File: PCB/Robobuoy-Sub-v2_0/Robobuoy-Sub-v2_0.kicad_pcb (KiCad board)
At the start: 4 copper layers, 80 x 104.1 mm, 141 parts, among them J101 PROG/JTAG, J102 PUSH BUTTON, J103 RS232_Option, J104 ESC_BB, J105 ESC_SB, J106 Compass, J201 Accu 1, J202 LoadbalanceAccu1, J203 LoadbalanceAccu2, J204 CHARGE/ON-OFF, J205 Accu 2, J206 ESCSB, J207 ESCBB, Q101 AO3400A, Q102 AO3400A, Q201 AO3400A, Q202 AO3400A, Q203 AO3400A, Q204 AO3400A, Q205 AO3400A, Q206 AO3400A, Q207 AO3400A, Q208 AO3400A, SW101 ~{BOOT}, SW102 ~{RESET}, SW103 MODE, SW201 On/Off, U101 ESP32-WROOM-32E_(visible_peri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, U102 USBLC6-4SC6, U103 LSM303AGRTR, U104 LTC4311, U105 SN74LV1T34DBV, U106 SN74LV1T34DBV, U201 TPS5430DDAR, U202 SN74LV1T34DBV, U203 SN74LV1T34DBV, U204 TLV61046ADB

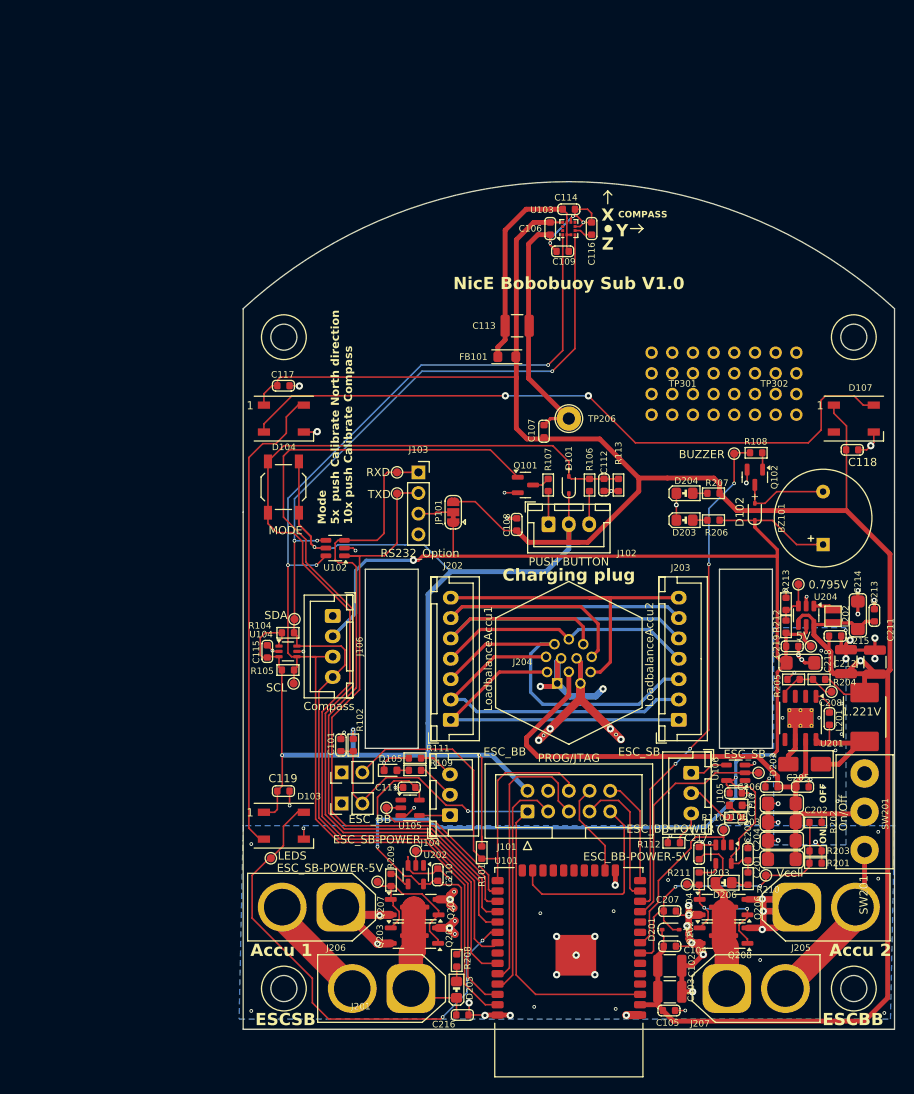
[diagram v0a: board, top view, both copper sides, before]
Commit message: Struct re defined. not finished yet
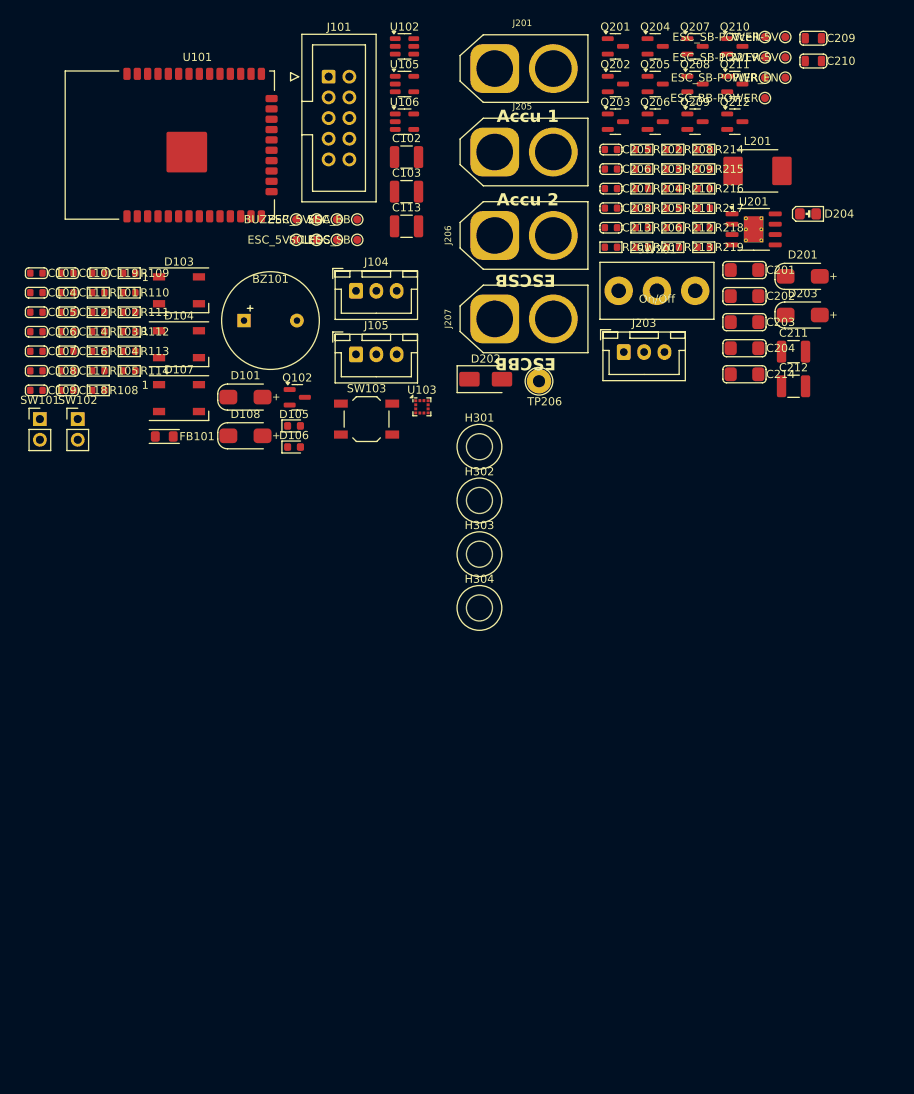
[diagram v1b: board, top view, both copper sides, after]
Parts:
- removed C115, C215, C216, C217, C219: 100n, A_Device:C_0603
- removed C218: 4.7uF/10V, A_Device:C_1206_(1.6)
- removed D102: 1N4148WS, A_Device:D_SOD-323_1.8x1.4x1.15
- removed D205: ESC_BB, A_Passive:LED_0805
- removed D206: ESC_SB, A_Passive:LED_0805
- removed J102: PUSH BUTTON, Connector_JST:JST_XH_B3B-XH-A_1x03_P2.50mm_Vertical
- removed J103: RS232_Option, Connector_PinSocket_2.54mm:PinSocket_1x04_P2.54mm_Vertical
- removed J106: Compass, Connector_JST:JST_XH_B4B-XH-A_1x04_P2.50mm_Vertical
- removed J202: LoadbalanceAccu1, Connector_JST:JST_XH_B7B-XH-A_1x07_P2.50mm_Vertical
- removed J204: CHARGE/ON-OFF, A_Connector:T4140012121000
- removed JP101: 5V/3.3V, Jumper:SolderJumper-3_P1.3mm_Bridged12_RoundedPad1.0x1.5mm
- removed L202: 10uH, A_Device:FTC252012S
- removed Q101: AO3400A, Package_TO_SOT_SMD:SOT-23
- removed R106, R107: 100, A_Device:R_0603
- removed TP209: 0.795V, A_Pads_Pins:Testpad_1
- removed TP210: 5V, A_Pads_Pins:Testpad_1
- removed TP301: RW1, A_Misc:ReworkPins
- removed TP302: RW2, A_Misc:ReworkPins
- removed U104: LTC4311, Package_TO_SOT_SMD:Texas_R-PDSO-G6
- removed U202, U203: SN74LV1T34DBV, Package_TO_SOT_SMD:SOT-23-5
- removed U204: TLV61046ADB, Package_TO_SOT_SMD:SOT-23-6
- added D108: SS14, A_Device:D_SMA_4.3x3x2.4, F.Cu at (86.1, 70.0)
- added Q209: AO3401A, Package_TO_SOT_SMD:SOT-23, F.Cu at (141.3, 31.4)
- added Q210: AO3401A, Package_TO_SOT_SMD:SOT-23, F.Cu at (146.2, 22.2)
- added Q211: AO3401A, Package_TO_SOT_SMD:SOT-23, F.Cu at (146.2, 26.8)
- added Q212: AO3400A, Package_TO_SOT_SMD:SOT-23, F.Cu at (146.2, 31.4)
- added R103: 100, A_Device:R_0603, F.Cu at (68.0, 57.2)
- added R114: 100, A_Device:R_0603, F.Cu at (71.8, 62.0)
- added R214: 10K, A_Device:R_0603, F.Cu at (142.4, 34.8)
- added R215: 10K, A_Device:R_0603, F.Cu at (142.4, 37.2)
- added R216: 100K, A_Device:R_0603, F.Cu at (142.4, 39.6)
- added R217: 100, A_Device:R_0603, F.Cu at (142.4, 42.0)
- added R218: 100K, A_Device:R_0603, F.Cu at (142.4, 44.4)
- added R219: 100K, A_Device:R_0603, F.Cu at (142.4, 46.8)
- added TP205: ESC_SB-POWER-5V, A_Pads_Pins:Testpad_1, F.Cu at (152.4, 21.0)
- C209, C210: value 100n -> 10u/25V; footprint A_Device:C_0603 -> A_Device:C_0805
- D101, D201: value 1N4148WS -> SS14; footprint A_Device:D_SOD-323_1.8x1.4x1.15 -> A_Device:D_SMA_4.3x3x2.4
- D106: value PWR_ESC_BB -> PWR_ESC_SB
- D203: value 5V -> SS14; footprint A_Passive:LED_0805 -> A_Device:D_SMA_4.3x3x2.4
- J203: value LoadbalanceAccu2 -> CHRG_DATA; footprint Connector_JST:JST_XH_B7B-XH-A_1x07_P2.50mm_Vertical -> Connector_JST:JST_XH_B3B-XH-A_1x03_P2.50mm_Vertical
- Q203, Q204, Q205, Q206, Q207, Q208: value AO3400A -> AO3401A
- R109, R110: value 1.8k -> 4.7k
- R206, R210: value 1.8k -> 10K
- R207: value 1k -> 100
- R208: value 1.8k -> 100K
- R211: value 100 -> 10K
- R212: value 82K -> 100K
- R213: value 15K -> 100K
- TP102: value RXD -> ESC_5V
- TP103: value TXD -> ESC_5V
- TP208: value ESC_BB-POWER-5V -> PWR_EN
- moved C105 115.7 mm to (60.4, 54.8)
- moved TP207 113.0 mm to (152.4, 23.5)
- moved U101 112.8 mm to (76.8, 34.3), turned to 0 degrees
- moved Q207 111.8 mm to (141.3, 22.2)
- moved C104 111.8 mm to (60.4, 52.4)
- moved Q201 111.6 mm to (131.5, 22.2), turned to 0 degrees
- moved C210 110.1 mm to (155.8, 24.0), turned to 0 degrees
- moved Q204 105.9 mm to (136.4, 22.2)
- moved Q202 105.2 mm to (131.5, 26.8)
- moved Q205 104.8 mm to (136.4, 26.8), turned to 0 degrees
- moved Q208 104.7 mm to (141.3, 26.8), turned to 0 degrees
- moved J201 104.7 mm to (116.7, 24.9), turned to 0 degrees
- moved C102 104.5 mm to (105.9, 35.8)
- moved TP203 104.2 mm to (149.9, 26.0)
- moved C110 104.0 mm to (64.2, 50.0)
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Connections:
- net /CPU/SCL renamed Net-(U101-SCL/GPIO22)
- net /CPU/SDA renamed Net-(U101-SDA/GPIO21)
- BZ101 pad 1: +5V -> +3.3V
- C110 pad 1: +5V -> Net-(J105-Pin_2)
- C110 pad 2: GND -> Net-(D106-K)
- C111 pad 1: +5V -> Net-(J104-Pin_2)
- C111 pad 2: GND -> Net-(D105-K)
- C201 pad 1: +VSW -> Vbatt
- C202 pad 1: +VSW -> Vbatt
- C203 pad 1: +VSW -> Vbatt
- C204 pad 1: +VSW -> Vbatt
- C205 pad 1: +VSW -> Vbatt
- C206 pad 1: +VSW -> Vbatt
- C209 pad 1: +5V -> Net-(D203-K)
- C210 pad 1: +5V -> Net-(D203-K)
- D101 pad 2: BUTTON -> Net-(BZ101--)
- D105 pad 1: GND -> Net-(D105-K)
- D106 pad 1: GND -> Net-(D106-K)
- D203 pad 1: GND -> Net-(D203-K)
- D203 pad 2: Net-(D203-A) -> /CPU/COM
- J104 pad 3: Net-(J104-Pin_3) -> Net-(D105-K)
- J105 pad 3: Net-(J105-Pin_3) -> Net-(D106-K)
- J203 pad 1: Net-(J202-Pin_1) -> GND
- J203 pad 2: Net-(J202-Pin_2) -> /CPU/COM
- J203 pad 3: Net-(J202-Pin_3) -> Vbatt
- J206 pad 1: Net-(D205-K) -> GND
- J206 pad 2: Vbatt -> Net-(J206-Pin_2)
- J207 pad 1: Net-(D206-K) -> GND
- J207 pad 2: Vbatt -> Net-(J207-Pin_2)
- Q201 pad 3: Net-(D205-K) -> Net-(Q201-D)
- Q202 pad 3: Net-(D206-K) -> Net-(Q202-D)
- Q203 pad 1: Net-(Q201-G) -> Net-(Q203-G)
- Q203 pad 2: GND -> Vbatt
- Q203 pad 3: Net-(D205-K) -> Net-(J206-Pin_2)
- Q204 pad 1: Net-(Q202-G) -> Net-(Q204-G)
- Q204 pad 2: GND -> Vbatt
- Q204 pad 3: Net-(D206-K) -> Net-(J207-Pin_2)
- Q205 pad 1: Net-(Q201-G) -> Net-(Q203-G)
- Q205 pad 2: GND -> Vbatt
- Q205 pad 3: Net-(D205-K) -> Net-(J206-Pin_2)
- Q206 pad 1: Net-(Q202-G) -> Net-(Q204-G)
- Q206 pad 2: GND -> Vbatt
- Q206 pad 3: Net-(D206-K) -> Net-(J207-Pin_2)
- Q207 pad 1: Net-(Q201-G) -> Net-(Q203-G)
- Q207 pad 2: GND -> Vbatt
- Q207 pad 3: Net-(D205-K) -> Net-(J206-Pin_2)
- Q208 pad 1: Net-(Q202-G) -> Net-(Q204-G)
- Q208 pad 2: GND -> Vbatt
- Q208 pad 3: Net-(D206-K) -> Net-(J207-Pin_2)
- R111 pad 2: Net-(J104-Pin_3) -> Net-(D105-K)
- R112 pad 2: Net-(J105-Pin_3) -> Net-(D106-K)
- R202 pad 1: +VSW -> Net-(Q211-D)
- R206 pad 1: +5V -> Net-(D204-A)
- R206 pad 2: Net-(D203-A) -> +3.3V
- R207 pad 1: Net-(D204-A) -> Net-(Q202-G)
- R207 pad 2: +3.3V -> /CPU/PWR_ESC_BB
- R208 pad 1: +5V -> Net-(D203-K)
- R208 pad 2: Net-(D205-A) -> GND
- R209 pad 2: Net-(U202-Y) -> /CPU/PWR_ESC_SB
- R210 pad 1: +5V -> Net-(Q202-D)
- R210 pad 2: Net-(D206-A) -> Net-(Q204-G)
- R211 pad 1: Net-(Q202-G) -> Vbatt
- R211 pad 2: Net-(U203-Y) -> Net-(Q204-G)
- R212 pad 1: +5V -> Net-(D203-K)
- R212 pad 2: Net-(U204-FB) -> Net-(R212-Pad2)
- R213 pad 1: Net-(U204-FB) -> Net-(R213-Pad1)
- R213 pad 2: GND -> Net-(R212-Pad2)
- SW201 pad 2: +VSW -> Net-(R216-Pad1)
- TP102 pad 1: Net-(J103-Pin_1) -> Net-(J104-Pin_2)
- TP103 pad 1: Net-(J103-Pin_2) -> Net-(J105-Pin_2)
- TP107 pad 1: ESC_BB -> Net-(U105-A)
- TP108 pad 1: ESC_SB -> Net-(U106-A)
- TP207 pad 1: Net-(Q201-G) -> Net-(Q203-G)
- TP208 pad 1: Net-(Q202-G) -> Net-(D203-K)
- U101 pad 27: Net-(J103-Pin_2) -> /CPU/VbatEn
- U101 pad 28: Net-(J103-Pin_1) -> /CPU/COM
- U101 pad 29: BUTTON_LIGHT -> unconnected-(U101-CS/GPIO5-Pad29)
- U102 pad 1: Net-(J103-Pin_2) -> /CPU/COM
- U102 pad 3: Net-(J103-Pin_1) -> /CPU/COM
- U105 pad 2: ESC_BB -> Net-(U105-A)
- U105 pad 3: GND -> Net-(D105-K)
- U105 pad 5: +5V -> Net-(J104-Pin_2)
- U106 pad 2: ESC_SB -> Net-(U106-A)
- U106 pad 3: GND -> Net-(D106-K)
- U106 pad 5: +5V -> Net-(J105-Pin_2)
- U201 pad 5: unconnected-(U201-ENA-Pad5) -> Net-(D203-K)
- U201 pad 7: +VSW -> Vbatt
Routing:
- net +3.3V: track 457.9 -> 0.00 mm, vias 5 -> 0
- net GND: track 247.7 -> 12.2 mm, vias 97 -> 0
- net +5V: track 231.5 -> 0.00 mm, vias 5 -> 0
- net Net-(U101-SCL/GPIO22): track 147.1 -> 0.00 mm, vias 3 -> 0
- net Net-(U101-SDA/GPIO21): track 140.7 -> 0.00 mm, vias 3 -> 0
- net BUTTON: track 129.5 -> 0.00 mm
- net BUTTON_LIGHT: track 108.5 -> 0.00 mm
- net Net-(D104-DOUT): track 84.7 -> 0.00 mm, vias 2 -> 0
- net Net-(J103-Pin_1): track 82.4 -> 0.00 mm
- net Net-(J103-Pin_2): track 77.1 -> 0.00 mm
- net +VSW: track 72.0 -> 0.00 mm
- net EN: track 68.8 -> 0.00 mm, vias 1 -> 0
- net BUZZER: track 62.4 -> 0.00 mm, vias 4 -> 0
- net LEDS: track 60.2 -> 0.00 mm, vias 2 -> 0
- net Vbatt: track 189.9 -> 130.0 mm, vias 6 -> 0
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- removed copper zone on B.Cu, net GND
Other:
- board outline removed
- board text removed: "COMPASS"
- board text removed: "Charging plug"
- board text removed: "Mode 5x push Calibrate North direction 10x push Calibrate Compass"
- board text removed: "NicE Bobobuoy Sub V1.0"
- board text removed: "OFF"
- board text removed: "ON"
- board text removed: "X"
- board text removed: "Y"
- board text removed: "Z"

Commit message: Many changes
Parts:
- removed C118, C119: 100n, A_Device:C_0603
- removed D104, D107: WS2812B, LED_SMD:LED_WS2812B_PLCC4_5.0x5.0mm_P3.2mm
- removed D106: PWR_ESC_SB, LED_SMD:LED_0603_1608Metric
- removed D108: SS14, A_Device:D_SMA_4.3x3x2.4
- removed H301, H302, H303, H304: MountingHole, A_Mechanical:NPTH_M3
- removed J104: ESC_BB, Connector_JST:JST_XH_B3B-XH-A_1x03_P2.50mm_Vertical
- removed J105: ESC_SB, Connector_JST:JST_XH_B3B-XH-A_1x03_P2.50mm_Vertical
- removed J201: Accu 1, A_Connector:AMASS_XT60-M_1x02_P7.20mm_Vertical
- removed J203: CHRG_DATA, Connector_JST:JST_XH_B3B-XH-A_1x03_P2.50mm_Vertical
- removed J205: Accu 2, A_Connector:AMASS_XT60-M_1x02_P7.20mm_Vertical
- removed J206: ESCSB, A_Connector:AMASS_XT60-F_1x02_P7.20mm_Vertical
- removed J207: ESCBB, A_Connector:AMASS_XT60-F_1x02_P7.20mm_Vertical
- removed Q102, Q212: AO3400A, Package_TO_SOT_SMD:SOT-23
- removed Q203, Q204, Q205, Q206, Q207, Q208, Q209, Q210, Q211: AO3401A, Package_TO_SOT_SMD:SOT-23
- removed R108, R111, R112, R114, R217: 100, A_Device:R_0603
- removed R109, R110: 4.7k, A_Device:R_0603
- removed R113, R214, R215: 10K, A_Device:R_0603
- removed R216, R218, R219: 100K, A_Device:R_0603
- removed TP105: SDA, A_Pads_Pins:Testpad_1
- removed TP106: LEDS, A_Pads_Pins:Testpad_1
- removed TP107: ESC_BB, A_Pads_Pins:Testpad_1
- removed TP108: ESC_SB, A_Pads_Pins:Testpad_1
- removed TP205, TP207: ESC_SB-POWER-5V, A_Pads_Pins:Testpad_1
- removed TP206: GND, TestPoint:TestPoint_Loop_D2.54mm_Drill1.5mm_Beaded
- removed TP208: PWR_EN, A_Pads_Pins:Testpad_1
- removed U105, U106: SN74LV1T34DBV, Package_TO_SOT_SMD:SOT-23-5
- added C401: 100n, A_Device:C_0603, F.Cu at (256.3, 49.9)
- added C402: 100n, A_Device:C_0603, F.Cu at (246.4, 62.2)
- added C403: 100n, A_Device:C_0603, F.Cu at (277.2, 92.5)
- added C404: 100n, A_Device:C_0603, F.Cu at (245.8, 112.5)
- added D102: WS2812B, LED_SMD:LED_WS2812B_PLCC4_5.0x5.0mm_P3.2mm, F.Cu at (129.5, 143.8)
- added D205: 3.3V, A_Passive:LED_0805, F.Cu at (61.9, 106.2)
- added D401: SS14, A_Device:D_SMA_4.3x3x2.4, F.Cu at (259.2, 45.9)
- added D402: PWR_ESC_BB, LED_SMD:LED_0603_1608Metric, F.Cu at (246.4, 64.0)
- added D403: SS14, A_Device:D_SMA_4.3x3x2.4, F.Cu at (259.4, 94.9)
- added D404: PWR_ESC_BB, LED_SMD:LED_0603_1608Metric, F.Cu at (252.9, 111.7)
- added H501: MountingHole, A_Mechanical:NPTH_M3, F.Cu at (70.5, 108.1)
- added H502: MountingHole, A_Mechanical:NPTH_M3, F.Cu at (70.5, 114.7)
- added H503: MountingHole, A_Mechanical:NPTH_M3, F.Cu at (70.5, 121.3)
- added H504: MountingHole, A_Mechanical:NPTH_M3, F.Cu at (70.5, 127.9)
- added J102: Conn_01x03_Pin, Connector_Wire:SolderWire-0.75sqmm_1x03_P4.8mm_D1.25mm_OD2.3mm, F.Cu at (141.2, 132.2)
- added J103: Conn_01x03_Pin, Connector_Wire:SolderWire-0.75sqmm_1x03_P4.8mm_D1.25mm_OD2.3mm, F.Cu at (136.0, 140.7)
- added J202: CHRG/DATA, Connector_Wire:SolderWire-0.75sqmm_1x03_P4.8mm_D1.25mm_OD2.3mm, F.Cu at (53.2, 129.6)
- added J401: PWR_ESC_SB, Connector_Wire:SolderWire-0.75sqmm_1x02_P4.8mm_D1.25mm_OD2.3mm, F.Cu at (245.4, 45.9)
- added J402: ESC_SB, Connector_JST:JST_XH_B3B-XH-A_1x03_P2.50mm_Vertical, F.Cu at (250.3, 58.4)
- added J403: INPUT_BB, Connector_Wire:SolderWire-0.75sqmm_1x03_P4.8mm_D1.25mm_OD2.3mm, F.Cu at (264.8, 99.7)
- added J404: INPUT_SB, Connector_Wire:SolderWire-0.75sqmm_1x03_P4.8mm_D1.25mm_OD2.3mm, F.Cu at (264.8, 50.7)
- added J405: ESC_BB, Connector_JST:JST_XH_B3B-XH-A_1x03_P2.50mm_Vertical, F.Cu at (250.3, 106.4)
- added J406: ESCBB, Connector_Wire:SolderWire-0.75sqmm_1x02_P4.8mm_D1.25mm_OD2.3mm, F.Cu at (245.4, 94.9)
- added MOD401: Balanced 6S BMS, A_Module:BMS_6S_14A, F.Cu at (209.8, 46.9)
- added MOD402: ~, A_Mechanical:Accupack_6C, F.Cu at (210.8, 45.9)
- added MOD403: ~, A_Mechanical:Accupack_6C, F.Cu at (210.8, 94.9)
- added MOD404: Balanced 6S BMS, A_Module:BMS_6S_14A, F.Cu at (209.8, 94.9)
- added Q101: AO3400A, Package_TO_SOT_SMD:SOT-23, F.Cu at (146.9, 124.5)
- added Q401: AO3400A, Package_TO_SOT_SMD:SOT-23, F.Cu at (258.8, 49.9)
- added Q402: AO3401A, Package_TO_SOT_SMD:SOT-23, F.Cu at (254.4, 40.8)
- added Q403: AO3401A, Package_TO_SOT_SMD:SOT-23, F.Cu at (243.7, 40.8)
- added Q404: AO3401A, Package_TO_SOT_SMD:SOT-23, F.Cu at (247.3, 40.8)
- added Q405: AO3401A, Package_TO_SOT_SMD:SOT-23, F.Cu at (250.8, 40.8)
- added Q406: AO3401A, Package_TO_SOT_SMD:SOT-23, F.Cu at (258.0, 40.8)
- added Q407: AO3400A, Package_TO_SOT_SMD:SOT-23, F.Cu at (272.8, 89.1)
- added Q408: AO3401A, Package_TO_SOT_SMD:SOT-23, F.Cu at (243.7, 88.9)
- added Q409: AO3401A, Package_TO_SOT_SMD:SOT-23, F.Cu at (247.3, 88.9)
- added Q410: AO3401A, Package_TO_SOT_SMD:SOT-23, F.Cu at (250.8, 88.9)
- added Q411: AO3401A, Package_TO_SOT_SMD:SOT-23, F.Cu at (254.4, 88.9)
- added Q412: AO3401A, Package_TO_SOT_SMD:SOT-23, F.Cu at (257.9, 88.9)
- added R106: 100, A_Device:R_0603, F.Cu at (109.5, 144.6)
- added R401: 100, A_Device:R_0603, F.Cu at (254.8, 47.0)
- added R402: 100K, A_Device:R_0603, F.Cu at (254.8, 49.9)
- added R403: 10K, A_Device:R_0603, F.Cu at (260.8, 40.9)
- added R404: 18K, A_Device:R_0603, F.Cu at (240.2, 45.9)
- added R405: 100, A_Device:R_0603, F.Cu at (265.5, 55.1)
- added R406: 4.7k, A_Device:R_0603, F.Cu at (249.4, 64.0)
- added R407: 100, A_Device:R_0603, F.Cu at (238.8, 57.1)
- added R408: 100K, A_Device:R_0603, F.Cu at (263.9, 55.1)
- added R409: 100, A_Device:R_0603, F.Cu at (272.7, 83.6)
- added R410: 100K, A_Device:R_0603, F.Cu at (277.2, 99.8)
- added R411: 100, A_Device:R_0603, F.Cu at (277.2, 102.2)
- added R412: 10K, A_Device:R_0603, F.Cu at (260.9, 90.1)
- added R413: 100K, A_Device:R_0603, F.Cu at (281.0, 95.0)
- added R414: 18K, A_Device:R_0603, F.Cu at (239.5, 93.7)
- added R415: 4.7k, A_Device:R_0603, F.Cu at (245.9, 110.4)
- added R416: 100, A_Device:R_0603, F.Cu at (238.9, 105.7)
- added TP401: ESC_BB-POWER, A_Pads_Pins:Testpad_1, F.Cu at (253.2, 46.3)
- added TP402: ESC_SB-POWER-5V, A_Pads_Pins:Testpad_1, F.Cu at (240.1, 47.8)
- added TP403: ESC_BB, A_Pads_Pins:Testpad_1, F.Cu at (262.1, 55.8)
- added TP404: ESC_5V, A_Pads_Pins:Testpad_1, F.Cu at (250.2, 65.9)
- added TP405: ESC_BB-POWER, A_Pads_Pins:Testpad_1, F.Cu at (284.1, 100.4)
- added TP406: ESC_BB, A_Pads_Pins:Testpad_1, F.Cu at (284.1, 102.9)
- added TP407: ESC_SB-POWER-5V, A_Pads_Pins:Testpad_1, F.Cu at (284.1, 105.4)
- added TP408: ESC_5V, A_Pads_Pins:Testpad_1, F.Cu at (284.1, 107.9)
- added U401: SN74LV1T34DBV, Package_TO_SOT_SMD:SOT-23-5, F.Cu at (264.5, 59.1)
- added U402: SN74LV1T34DBV, Package_TO_SOT_SMD:SOT-23-5, F.Cu at (288.0, 110.9)
- C102, C103, C113: value 100u/10V -> 100n; footprint Capacitor_SMD:C_1210_3225Metric -> A_Device:C_0603
- C105, C106, C114: value 100n -> 100u/10V; footprint A_Device:C_0603 -> Capacitor_SMD:C_1210_3225Metric
- C117: value 100n -> 10n
- C208: value 10n -> 10u/25V; footprint A_Device:C_0603 -> A_Device:C_0805
- C210: value 10u/25V -> 10n; footprint A_Device:C_0805 -> A_Device:C_0603
- D101: value SS14 -> WS2812B; footprint A_Device:D_SMA_4.3x3x2.4 -> LED_SMD:LED_WS2812B_PLCC4_5.0x5.0mm_P3.2mm
- D105: value PWR_ESC_BB -> SS14; footprint LED_SMD:LED_0603_1608Metric -> A_Device:D_SMA_4.3x3x2.4
- D202: value B340A -> SS14; footprint Diode_SMD:D_SMA -> A_Device:D_SMA_4.3x3x2.4
- D204: value 3.3V -> SS54; footprint A_Passive:LED_0805 -> Diode_SMD:D_SMA
- Q202: value AO3400A -> AO3401A
- R103: value 100 -> 10K
- R201: value 1k -> 100
- R202: value 6.2k -> 100K
- R203: value 1k -> 100K
- R204: value 18K -> 1k
- R205, R210: value 10K -> 100K
- R206: value 10K -> 6.2k
- R207, R209: value 100 -> 100K
- R208: value 100K -> 1k
- R211: value 10K -> 18K
- R212, R213: value 100K -> 10K
- TP101: value BUZZER -> LEDS
- TP102: value ESC_5V -> BUZZER
- TP103: value ESC_5V -> SDA
- TP201: value Vcell -> PWR_EN
- TP202: value 1.221V -> Vcell
- TP203: value ESC_SB-POWER -> GND; footprint A_Pads_Pins:Testpad_1 -> TestPoint:TestPoint_Loop_D2.54mm_Drill1.5mm_Beaded
- TP204: value ESC_BB-POWER -> 1.221V
- U102: value USBLC6-4SC6 -> LSM303AGRTR; footprint Package_TO_SOT_SMD:SOT-23-6 -> Package_LGA:LGA-12_2x2mm_P0.5mm
- U103: value LSM303AGRTR -> USBLC6-4SC6; footprint Package_LGA:LGA-12_2x2mm_P0.5mm -> Package_TO_SOT_SMD:SOT-23-6
- moved TP201 153.2 mm to (42.7, 130.5)
- moved TP202 153.2 mm to (42.7, 133.0)
- moved TP204 151.4 mm to (42.7, 135.5)
- moved C210 150.3 mm to (34.9, 113.2)
- moved L201 141.9 mm to (37.7, 125.4)
- moved U201 141.9 mm to (37.2, 132.6)
- moved C209 141.3 mm to (60.8, 125.8)
- moved TP203 140.0 mm to (61.4, 134.5)
- moved Q201 138.3 mm to (46.8, 131.5)
- moved Q202 138.3 mm to (46.8, 136.1)
- moved D204 135.8 mm to (54.8, 134.2)
- moved R202 131.5 mm to (34.9, 120.4)
- moved U102 130.5 mm to (106.8, 152.6)
- moved R208 130.0 mm to (38.7, 118.0)
- moved R209 130.0 mm to (38.7, 120.4)
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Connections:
- C109 pad 1: Net-(U103-CS_MAG) -> +3.3V
- C110 pad 1: Net-(J105-Pin_2) -> +3.3V
- C110 pad 2: Net-(D106-K) -> GND
- C111 pad 1: Net-(J104-Pin_2) -> +3.3V
- C111 pad 2: Net-(D105-K) -> GND
- C113 pad 1: Net-(U103-CS_MAG) -> Net-(U102-CS_MAG)
- C114 pad 1: Net-(U103-CS_MAG) -> Net-(U102-CS_MAG)
- C116 pad 1: Net-(U103-C1) -> Net-(U102-C1)
- C117 pad 1: +3.3V -> GND
- C117 pad 2: GND -> Net-(U102-CS_MAG)
- C208 pad 1: Net-(D202-K) -> Net-(D201-K)
- C208 pad 2: Net-(U201-BOOT) -> GND
- C209 pad 1: Net-(D203-K) -> Net-(D201-K)
- C210 pad 1: Net-(D203-K) -> Net-(D204-K)
- C210 pad 2: GND -> Net-(U201-BOOT)
- D101 pad 2: Net-(BZ101--) -> Net-(D101-DOUT)
- D103 pad 2: Net-(D103-DOUT) -> unconnected-(D103-DOUT-Pad2)
- D103 pad 4: LEDS -> Net-(D102-DOUT)
- D105 pad 1: Net-(D105-K) -> +3.3V
- D105 pad 2: Net-(D105-A) -> Net-(BZ101--)
- D201 pad 1: +3.3V -> Net-(D201-K)
- D201 pad 2: /CPU/Vsamp -> /CPU/PwrEn
- D202 pad 1: Net-(D202-K) -> +3.3V
- D202 pad 2: GND -> /CPU/Vsamp
- D203 pad 1: Net-(D203-K) -> Net-(D201-K)
- D204 pad 1: GND -> Net-(D204-K)
- D204 pad 2: Net-(D204-A) -> GND
- FB101 pad 2: Net-(U103-CS_MAG) -> Net-(U102-CS_MAG)
- L201 pad 1: Net-(D202-K) -> Net-(D204-K)
- Q202 pad 2: GND -> Vbatt
- R103 pad 1: Net-(U105-A) -> BUTTON
- R103 pad 2: ESC_BB -> GND
- R201 pad 1: /CPU/Vsamp -> Net-(Q201-G)
- R201 pad 2: GND -> /CPU/VbatEn
- R202 pad 1: Net-(Q211-D) -> Net-(Q202-G)
- R202 pad 2: /CPU/Vsamp -> Vbatt
- R203 pad 1: /CPU/Vsamp -> Net-(Q201-D)
- R203 pad 2: GND -> Net-(Q202-G)
- R204 pad 1: +3.3V -> /CPU/Vsamp
- R204 pad 2: Net-(U201-Vsens) -> GND
- R205 pad 1: Net-(U201-Vsens) -> Net-(R205-Pad1)
- R205 pad 2: GND -> Net-(R205-Pad2)
- R206 pad 1: Net-(D204-A) -> Net-(Q202-D)
- R206 pad 2: +3.3V -> /CPU/Vsamp
- R207 pad 1: Net-(Q202-G) -> Net-(R205-Pad2)
- R207 pad 2: /CPU/PWR_ESC_BB -> Net-(R207-Pad2)
- R208 pad 1: Net-(D203-K) -> /CPU/Vsamp
- R209 pad 1: Net-(Q201-G) -> Net-(D201-K)
- R209 pad 2: /CPU/PWR_ESC_SB -> Net-(R207-Pad2)
- R210 pad 1: Net-(Q202-D) -> Net-(D201-K)
- R210 pad 2: Net-(Q204-G) -> GND
- R211 pad 1: Vbatt -> +3.3V
- R211 pad 2: Net-(Q204-G) -> Net-(U201-Vsens)
- R212 pad 1: Net-(D203-K) -> Net-(U201-Vsens)
- R212 pad 2: Net-(R212-Pad2) -> GND
- R213 pad 2: Net-(R212-Pad2) -> +3.3V
- SW201 pad 2: Net-(R216-Pad1) -> Net-(R205-Pad1)
- TP101 pad 1: BUZZER -> LEDS
- TP102 pad 1: Net-(J104-Pin_2) -> BUZZER
- TP103 pad 1: Net-(J105-Pin_2) -> Net-(U101-SDA/GPIO21)
- TP201 pad 1: /CPU/Vsamp -> Net-(D201-K)
- TP202 pad 1: Net-(U201-Vsens) -> /CPU/Vsamp
- TP203 pad 1: /CPU/PWR_ESC_SB -> GND
- TP204 pad 1: /CPU/PWR_ESC_BB -> Net-(U201-Vsens)
- U101 pad 10: unconnected-(U101-GPIO25-Pad10) -> ESC_BB
- U101 pad 26: ESC_BB -> /CPU/PwrEn
- U101 pad 37: /CPU/PWR_ESC_SB -> unconnected-(U101-MOSI/GPIO23-Pad37)
- U101 pad 8: /CPU/PWR_ESC_BB -> unconnected-(U101-GPIO32-Pad8)
- U102 pad 1: /CPU/COM -> Net-(U101-SCL/GPIO22)
- U102 pad 2: GND -> Net-(U102-CS_MAG)
- U102 pad 3: /CPU/COM -> Net-(U102-CS_MAG)
- U102 pad 5: +3.3V -> Net-(U102-C1)
- U102 pad 6: Net-(U101-SCL/GPIO22) -> GND
- U103 pad 1: Net-(U101-SCL/GPIO22) -> /CPU/COM
- U103 pad 2: Net-(U103-CS_MAG) -> GND
- U103 pad 3: Net-(U103-CS_MAG) -> /CPU/COM
- U103 pad 4: Net-(U101-SDA/GPIO21) -> ESC_BB
- U103 pad 5: Net-(U103-C1) -> +3.3V
- U103 pad 6: GND -> ESC_SB
- U201 pad 5: Net-(D203-K) -> Net-(D201-K)
- U201 pad 8: Net-(D202-K) -> Net-(D204-K)
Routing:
- net Vbatt: track 130.0 -> 0.00 mm
- net B-: track 0.00 -> 92.4 mm
- net B1: track 0.00 -> 85.7 mm
- net B5: track 0.00 -> 67.2 mm
- net B4: track 0.00 -> 53.0 mm
- net GND2: track 0.00 -> 48.6 mm
- net B2: track 0.00 -> 43.9 mm, vias 0 -> 2
- net VbattSB: track 0.00 -> 43.2 mm
- net B+: track 0.00 -> 35.2 mm
- net Net-(Q402-G): track 0.00 -> 34.7 mm
- net B3: track 0.00 -> 33.7 mm
- net Net-(D402-K): track 0.00 -> 32.2 mm
- net Net-(J402-Pin_2): track 0.00 -> 30.6 mm
- net Net-(J401-Pin_2): track 0.00 -> 23.2 mm
- net Net-(D401-A): track 0.00 -> 14.6 mm
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- removed copper zone on In1.Cu, net GND
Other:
- board outline added: 261.1 x 137.9 mm
- copper layers 4 -> 2

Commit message: Pcb changes
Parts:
- removed C117: 10n, A_Device:C_0603
- removed C212: 100u/10V, Capacitor_SMD:C_1210_3225Metric
- removed C213, C402, C403, C404: 100n, A_Device:C_0603
- removed C214: 4.7uF/10V, A_Device:C_1206_(1.6)
- removed D105, D403: SS14, A_Device:D_SMA_4.3x3x2.4
- removed D402, D404: PWR_ESC_BB, LED_SMD:LED_0603_1608Metric
- removed J102, J103: Conn_01x03_Pin, Connector_Wire:SolderWire-0.75sqmm_1x03_P4.8mm_D1.25mm_OD2.3mm
- removed J403: INPUT_BB, Connector_Wire:SolderWire-0.75sqmm_1x03_P4.8mm_D1.25mm_OD2.3mm
- removed J404: INPUT_SB, Connector_Wire:SolderWire-0.75sqmm_1x03_P4.8mm_D1.25mm_OD2.3mm
- removed J405: ESC_BB, Connector_JST:JST_XH_B3B-XH-A_1x03_P2.50mm_Vertical
- removed J406: ESCBB, Connector_Wire:SolderWire-0.75sqmm_1x02_P4.8mm_D1.25mm_OD2.3mm
- removed MOD401, MOD404: Balanced 6S BMS, A_Module:BMS_6S_14A
- removed MOD402, MOD403: ~, A_Mechanical:Accupack_6C
- removed Q407: AO3400A, Package_TO_SOT_SMD:SOT-23
- removed Q408, Q409, Q410, Q411, Q412: AO3401A, Package_TO_SOT_SMD:SOT-23
- removed R101, R412: 10K, A_Device:R_0603
- removed R404, R414: 18K, A_Device:R_0603
- removed R407, R409, R411, R416: 100, A_Device:R_0603
- removed R408, R410, R413: 100K, A_Device:R_0603
- removed R415: 4.7k, A_Device:R_0603
- removed SW101: ~{BOOT}, Connector_PinHeader_2.54mm:PinHeader_1x02_P2.54mm_Vertical
- removed TP402, TP407: ESC_SB-POWER-5V, A_Pads_Pins:Testpad_1
- removed TP404, TP408: ESC_5V, A_Pads_Pins:Testpad_1
- removed TP405: ESC_BB-POWER, A_Pads_Pins:Testpad_1
- removed TP406: ESC_BB, A_Pads_Pins:Testpad_1
- removed U402: SN74LV1T34DBV, Package_TO_SOT_SMD:SOT-23-5
- added C115: 10n, A_Device:C_0603, F.Cu at (100.8, 83.3)
- added C301: 100n, A_Device:C_0603, F.Cu at (45.8, 41.4)
- added D104: WS2812B, LED_SMD:LED_WS2812B_PLCC4_5.0x5.0mm_P3.2mm, F.Cu at (84.8, 68.4)
- added D301: PWR_ESC, LED_SMD:LED_0603_1608Metric, F.Cu at (41.8, 37.4)
- added J201: AccuSB, Connector_Wire:SolderWire-0.75sqmm_1x03_P4.8mm_D1.25mm_OD2.3mm, F.Cu at (86.5, 38.0)
- added J205: CHRG/DATA, Connector_Wire:SolderWire-0.75sqmm_1x03_P4.8mm_D1.25mm_OD2.3mm, F.Cu at (73.8, 28.4)
- added J301: ESC, Connector_JST:JST_XH_B3B-XH-A_1x03_P2.50mm_Vertical, F.Cu at (43.8, 28.4)
- added J302: ESC_PWR, Connector_Wire:SolderWire-0.75sqmm_1x02_P4.8mm_D1.25mm_OD2.3mm, F.Cu at (99.2, 33.2)
- added Q301: AO3400A, Package_TO_SOT_SMD:SOT-23, F.Cu at (80.8, 42.4)
- added Q302: AO3401A, Package_TO_SOT_SMD:SOT-23, F.Cu at (94.8, 33.8)
- added Q303: AO3401A, Package_TO_SOT_SMD:SOT-23, F.Cu at (94.8, 37.6)
- added Q304: AO3401A, Package_TO_SOT_SMD:SOT-23, F.Cu at (94.8, 41.5)
- added Q305: AO3401A, Package_TO_SOT_SMD:SOT-23, F.Cu at (99.2, 37.0)
- added Q306: AO3401A, Package_TO_SOT_SMD:SOT-23, F.Cu at (99.2, 40.8)
- added R301: 100K, A_Device:R_0603, F.Cu at (80.8, 45.3)
- added R302: 100, A_Device:R_0603, F.Cu at (42.8, 43.4)
- added R303: 10K, A_Device:R_0603, F.Cu at (84.5, 41.1)
- added R305: 18K, A_Device:R_0603, F.Cu at (91.6, 35.7)
- added R306: 4.7k, A_Device:R_0603, F.Cu at (44.8, 37.4)
- added TP301: ESC_PWM, A_Pads_Pins:Testpad_1, F.Cu at (47.8, 24.4)
- added TP303: ESC_5V, A_Pads_Pins:Testpad_1, F.Cu at (45.8, 39.4)
- added U301: SN74LV1T34DBV, Package_TO_SOT_SMD:SOT-23-5, F.Cu at (42.8, 40.4)
- C202, C204: value 4.7uF/10V -> 100n; footprint A_Device:C_1206_(1.6) -> A_Device:C_0603
- C203: value 4.7uF/10V -> 10n; footprint A_Device:C_1206_(1.6) -> A_Device:C_0603
- C205: value 100n -> 10u/25V; footprint A_Device:C_0603 -> A_Device:C_0805
- C206: value 10n -> 10u/25V; footprint A_Device:C_0603 -> A_Device:C_0805
- C207: value 100n -> 10n
- C208, C209: value 10u/25V -> 100u/10V; footprint A_Device:C_0805 -> Capacitor_SMD:C_1210_3225Metric
- C210: value 10n -> 100n
- C211: value 100u/10V -> 4.7uF/10V; footprint Capacitor_SMD:C_1210_3225Metric -> A_Device:C_1206_(1.6)
- D102: value WS2812B -> SM4007PL; footprint LED_SMD:LED_WS2812B_PLCC4_5.0x5.0mm_P3.2mm -> A_Device:D_SOD-123_2.85x1.8x1.3
- D201, D202, D203: value SS14 -> SM4007PL; footprint A_Device:D_SMA_4.3x3x2.4 -> A_Device:D_SOD-123_2.85x1.8x1.3
- D401: value SS14 -> PWR_ESC; footprint A_Device:D_SMA_4.3x3x2.4 -> LED_SMD:LED_0603_1608Metric
- J202: value CHRG/DATA -> AccuBB
- J401: value PWR_ESC_SB -> ESC; footprint Connector_Wire:SolderWire-0.75sqmm_1x02_P4.8mm_D1.25mm_OD2.3mm -> Connector_JST:JST_XH_B3B-XH-A_1x03_P2.50mm_Vertical
- J402: value ESC_SB -> ESC_PWR; footprint Connector_JST:JST_XH_B3B-XH-A_1x03_P2.50mm_Vertical -> Connector_Wire:SolderWire-0.75sqmm_1x02_P4.8mm_D1.25mm_OD2.3mm
- R103: value 10K -> 100
- R106: value 100 -> 10K
- R401: value 100 -> 100K
- R402: value 100K -> 100
- R405: value 100 -> 18K
- TP401: value ESC_BB-POWER -> ESC_PWM
- TP403: value ESC_BB -> ESC_5V
- moved R405 209.9 mm to (56.6, 35.3), turned to -90 degrees
- moved Q406 209.6 mm to (48.4, 41.5), turned to 90 degrees
- moved J402 203.5 mm to (48.4, 33.2), turned to 90 degrees
- moved Q405 202.5 mm to (48.4, 37.6), turned to 90 degrees
- moved Q402 201.7 mm to (52.9, 33.8), turned to 90 degrees
- moved R403 197.5 mm to (63.3, 41.3), turned to 180 degrees
- moved Q404 194.4 mm to (52.9, 41.5), turned to 90 degrees
- moved Q401 192.1 mm to (66.8, 42.5)
- moved Q403 190.9 mm to (52.9, 37.6), turned to 90 degrees
- moved R401 188.0 mm to (66.8, 45.4), turned to 0 degrees
- moved TP403 161.0 mm to (102.0, 38.9)
- moved U401 160.8 mm to (104.8, 40.4), turned to 90 degrees
- moved TP401 155.0 mm to (99.8, 24.4), turned to 0 degrees
- moved C401 154.7 mm to (101.8, 41.4)
- moved D401 153.8 mm to (105.6, 37.4), turned to 180 degrees
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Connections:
- net ESC_SB renamed /CPU/ESC_SB
- C112 pad 1: GND -> DR0
- C112 pad 2: BUTTON -> +3.3V
- C204 pad 1: Vbatt -> /CPU/Vsamp
- C205 pad 1: Vbatt -> Net-(D201-K)
- C206 pad 1: Vbatt -> Net-(D201-K)
- C207 pad 1: /CPU/Vsamp -> Net-(D204-K)
- C207 pad 2: GND -> Net-(U201-BOOT)
- C208 pad 1: Net-(D201-K) -> +3.3V
- C209 pad 1: Net-(D201-K) -> +3.3V
- C210 pad 1: Net-(D204-K) -> +3.3V
- C210 pad 2: Net-(U201-BOOT) -> GND
- C401 pad 1: Net-(Q401-G) -> Net-(J401-Pin_2)
- C401 pad 2: GND2 -> GND
- D102 pad 2: Net-(D102-DOUT) -> Net-(BZ101--)
- D103 pad 2: unconnected-(D103-DOUT-Pad2) -> Net-(D103-DOUT)
- D103 pad 4: Net-(D102-DOUT) -> Net-(D101-DOUT)
- D401 pad 1: Net-(D401-K) -> GND
- J202 pad 1: GND -> Vbatt
- J202 pad 2: /CPU/COM -> GND
- J202 pad 3: Vbatt -> GND
- J401 pad 1: GND2 -> Net-(J401-Pin_1)
- J402 pad 2: Net-(J402-Pin_2) -> GND
- Q401 pad 1: Net-(Q401-G) -> /CPU/ESC_PWR_BB
- Q401 pad 2: GND2 -> GND
- Q402 pad 2: VbattSB -> Vbatt
- Q402 pad 3: Net-(J401-Pin_2) -> Net-(J402-Pin_1)
- Q403 pad 2: VbattSB -> Vbatt
- Q403 pad 3: Net-(J401-Pin_2) -> Net-(J402-Pin_1)
- Q404 pad 2: VbattSB -> Vbatt
- Q404 pad 3: Net-(J401-Pin_2) -> Net-(J402-Pin_1)
- Q405 pad 2: VbattSB -> Vbatt
- Q405 pad 3: Net-(J401-Pin_2) -> Net-(J402-Pin_1)
- Q406 pad 2: VbattSB -> Vbatt
- Q406 pad 3: Net-(J401-Pin_2) -> Net-(J402-Pin_1)
- R103 pad 1: BUTTON -> Net-(Q101-G)
- R103 pad 2: GND -> BUZZER
- R106 pad 1: Net-(Q101-G) -> +3.3V
- R106 pad 2: BUZZER -> DR0
- R401 pad 1: Net-(Q401-G) -> /CPU/ESC_PWR_BB
- R401 pad 2: Net-(D401-K) -> GND
- R402 pad 1: Net-(Q401-G) -> Net-(U401-A)
- R402 pad 2: GND2 -> /CPU/ESC_BB
- R405 pad 1: Net-(U401-A) -> Vbatt
- R405 pad 2: Net-(D401-A) -> Net-(Q402-G)
- R406 pad 1: Net-(D402-A) -> Net-(D401-A)
- R406 pad 2: Net-(J402-Pin_2) -> Net-(J401-Pin_2)
- SW103 pad 1: BUTTON -> GND
- SW103 pad 2: +3.3V -> DR0
- TP401 pad 1: Net-(D401-K) -> Net-(J401-Pin_1)
- TP403 pad 1: Net-(U401-A) -> Net-(J401-Pin_2)
- U101 pad 10: ESC_BB -> /CPU/ESC_BB
- U101 pad 26: /CPU/PwrEn -> /CPU/VbatEn
- U101 pad 27: /CPU/VbatEn -> /CPU/PwrEn
- U101 pad 31: BUTTON -> unconnected-(U101-MISO/GPIO19-Pad31)
- U101 pad 8: unconnected-(U101-GPIO32-Pad8) -> /CPU/ESC_PWR_BB
- U101 pad 9: unconnected-(U101-GPIO33-Pad9) -> /CPU/ESC_PWR_SB
- U103 pad 4: ESC_BB -> /CPU/ESC_BB
- U401 pad 3: Net-(D402-K) -> GND
- U401 pad 4: Net-(J402-Pin_1) -> Net-(J401-Pin_1)
- U401 pad 5: Net-(J402-Pin_2) -> Net-(J401-Pin_2)
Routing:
- net GND: track 0.00 -> 382.9 mm, vias 0 -> 43
- net Vbatt: track 0.00 -> 281.0 mm
- net +3.3V: track 0.00 -> 196.3 mm, vias 0 -> 2
- net B-: track 92.4 -> 0.00 mm
- net B1: track 85.7 -> 0.00 mm
- net B5: track 67.2 -> 0.00 mm
- net Net-(U101-SDA/GPIO21): track 0.00 -> 62.4 mm, vias 0 -> 3
- net Net-(U101-SCL/GPIO22): track 0.00 -> 60.4 mm
- net /CPU/COM: track 0.00 -> 60.0 mm
- net B4: track 53.0 -> 0.00 mm
- net Net-(D201-K): track 0.00 -> 51.3 mm, vias 0 -> 4
- net GND2: track 48.6 -> 0.00 mm
- net DR0: track 0.00 -> 47.6 mm, vias 0 -> 2
- net BUZZER: track 0.00 -> 47.4 mm, vias 0 -> 2
- net B2: track 43.9 -> 0.00 mm, vias 2 -> 0
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- added copper zone on In1.Cu, net GND
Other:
- board size 261.1 x 137.9 mm -> 76 x 68 mm
- copper layers 2 -> 4
- board text added: "X"
- board text added: "Y"
- board text added: "Z"
- board text removed: "1 GND 2 Vbatt 3 MON_S7 4 MON_S6 5 MON_S5 6 MON_S4 7 MON_S3 8 MON_S2 9 MON_S1 10 +SW 11 Vbat 12 GND"
